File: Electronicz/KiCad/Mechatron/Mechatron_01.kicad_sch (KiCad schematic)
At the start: 47 parts, among them J1 Conn_01x15_Socket, J10 Servo_1, J11 Servo_2, J12 Servo_3, J13 V_ESP32, J14 GND_ESP32, J15 Motor_1, J16 Motor_2, J17 Motor_3, J18 Motor_4, J19 V_LED_2, J2 US_Sensor1, J20 V_LED_1, J21 V_LED_top, J22 GND_LED_top, J23 GND_LED_2, J24 GND_LED_1, J25 SD-Card-Reader, J26 Amplifier, J27 Speaker, J3 US_sensor_2, J4 US_sensor3, J5 US_sensor4, J6 US_sensor5, J7 US_sensor6, J8 GND_Battery, J9 V_Battery_Switch, Q1 LR_LED_Sensors, Q2 LR_3, Q3 LR_2, Q4 LR_1, Q5 LED_top, Q6 LED_2, Q7 LED_1

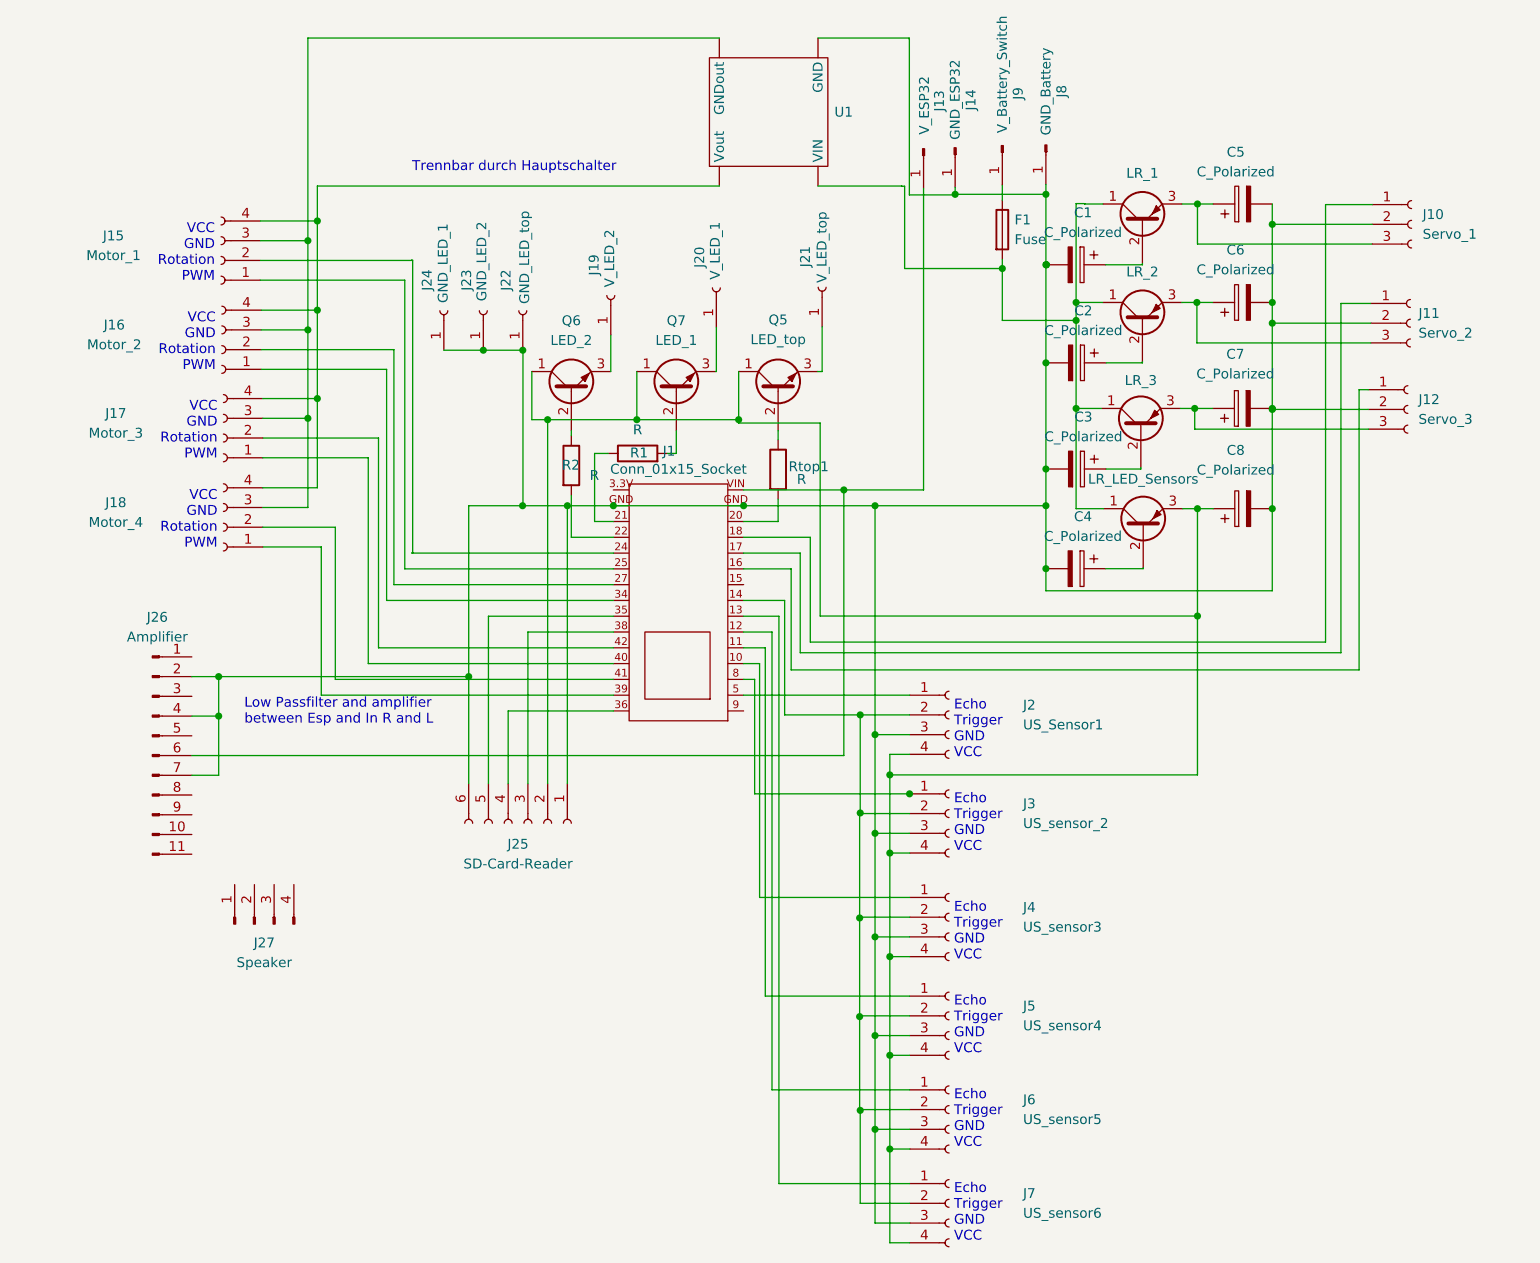
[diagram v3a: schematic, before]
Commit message: add filter and label of the Pin Header
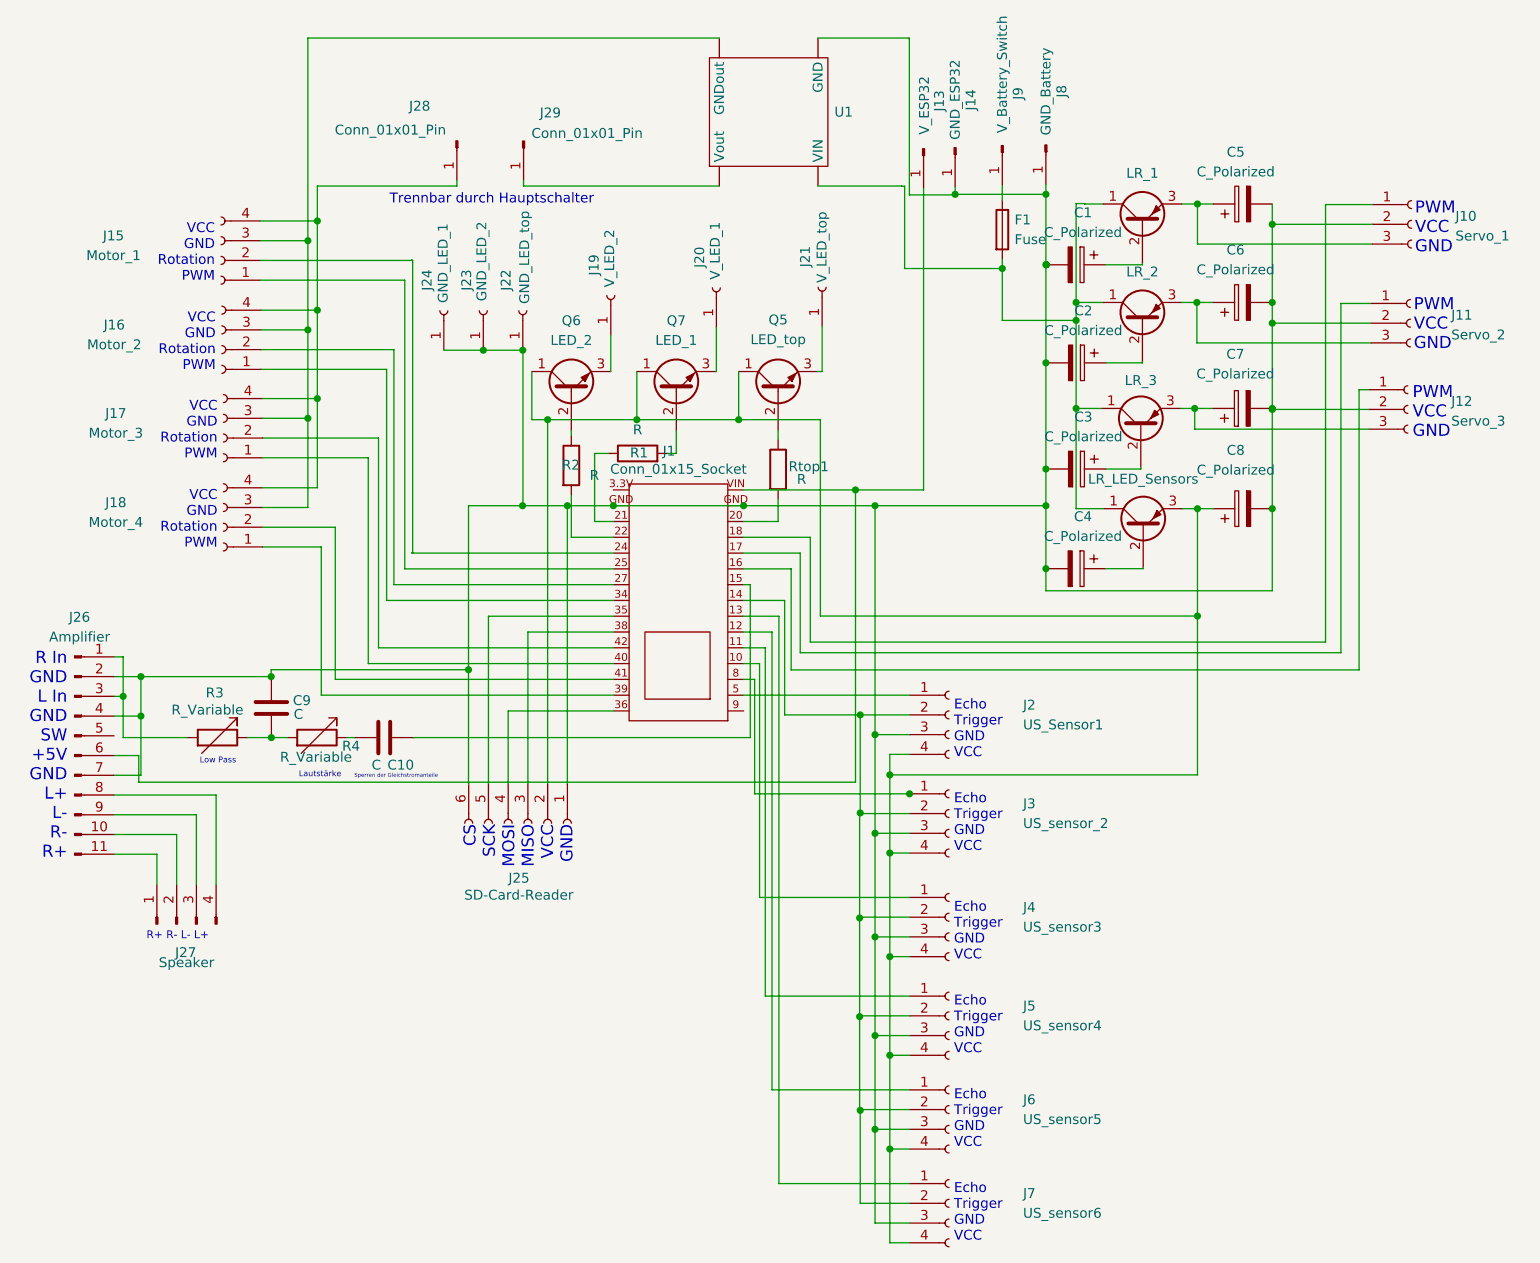
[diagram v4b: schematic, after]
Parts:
- added C10, C9: C, symbol Device:C
- added J28, J29: Conn_01x01_Pin, symbol Connector:Conn_01x01_Pin
- added R3, R4: R_Variable, symbol Device:R_Variable
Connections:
- net at J26.1 (Pin_1): now also J26.3 (Pin_3), R3.2
- net at J26.10 (Pin_10): now also J27.2 (Pin_2)
- net at J26.11 (Pin_11): now also J27.1 (Pin_1)
- net at C1.2, C2.2, C3.2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: now also C9.1
- net at J26.8 (Pin_8): now also J27.4 (Pin_4)
- net at J26.9 (Pin_9): now also J27.3 (Pin_3)
- net at J15.4 (Pin_4), J16.4 (Pin_4), J17.4 (Pin_4)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: now also J28.1 (Pin_1); no longer U1. (Vout)
- net at J1.15: now also C10.1
- new net: C10.2, R4.1
- new net: C9.2, R3.1, R4.2
- new net: J29.1 (Pin_1), U1. (Vout)
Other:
- note added: "CS SCK MOSI MISO VCC GND"
- note added: "Lautstärke"
- note added: "Low Pass"
- note added: "PWM VCC GND"
- note added: "R In GND L In GND SW +5V GND L+ L- R- R+"
- note added: "R+ R- L- L+"
- note added: "Sperren der Gleichstromanteile"
- note removed: "Low Passfilter and amplifier between Esp and In R and L"
- moved on the sheet: J26, J27

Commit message: Platinendesign
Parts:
- removed J26: Amplifier, symbol Connector:Conn_01x11_Pin
- removed J27: Speaker, symbol Connector:Conn_01x04_Pin
- added J26: AUDIOAMP, Connector_PinSocket_2.00mm:PinSocket_1x09_P2.00mm_Vertical, symbol Connector:Conn_01x09_Socket
- added J27: Speaker, Connector_PinHeader_2.54mm:PinHeader_1x02_P2.54mm_Vertical, symbol Connector:Conn_01x02_Pin
- added J30: SW, Connector_PinSocket_2.00mm:PinSocket_1x01_P2.00mm_Vertical, symbol Connector:Conn_01x01_Socket
- C1, C2, C3, C4, C5, C6, C7, C8: footprint (none) -> Capacitor_THT:C_Disc_D4.3mm_W1.9mm_P5.00mm
- C10, C9: footprint (none) -> Capacitor_THT:C_Disc_D3.0mm_W1.6mm_P2.50mm
- F1: footprint (none) -> Fuse:Fuseholder_Clip-5x20mm_Eaton_1A5601-01_Inline_P20.80x6.76mm_D1.70mm_Horizontal
- J28, J29: footprint (none) -> Connector_PinHeader_2.54mm:PinHeader_1x01_P2.54mm_Vertical
- Q1, Q2, Q3, Q4: footprint (none) -> Package_TO_SOT_THT:TO-126-3_Vertical
- R3: footprint (none) -> Potentiometer_THT:Potentiometer_Bourns_3386C_Horizontal
- R4: footprint (none) -> Resistor_THT:R_Axial_DIN0207_L6.3mm_D2.5mm_P10.16mm_Horizontal
- U1: footprint (none) -> Library:Spannungsregler
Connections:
- net at R3.2: now also J26.7 (Pin_7), J26.9 (Pin_9)
- net at C1.2, C2.2, C3.2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: now also U1.2 (GND), J26.3 (Pin_3), J26.6 (Pin_6), J26.8 (Pin_8); no longer U1. (Vout)
- net at J1.VIN, J13.1 (Pin_1): now also J26.4 (Pin_4)
- net at J15.3 (Pin_3), J16.3 (Pin_3), J17.3 (Pin_3)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: now also U1.4 (GNDout); no longer U1. (Vout)
- net at F1.2, Q1.1 (C), Q2.1 (C)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: now also U1.1 (VIN); no longer U1. (Vout)
- net at J29.1 (Pin_1): now also U1.3 (Vout); no longer U1. (Vout)
- new net: J26.1 (Pin_1), J27.1 (Pin_1)
- new net: J26.2 (Pin_2), J27.2 (Pin_2)
- new net: J26.5 (Pin_5), J30.1 (Pin_1)
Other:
- note added: "L- L+"
- note added: "R In GND L In GND SW +5V GND + -"
- note removed: "R In GND L In GND SW +5V GND L+ L- R- R+"
- note removed: "R+ R- L- L+"

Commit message: pcb design
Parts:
- J2: value US_Sensor1 -> Front
- J3: value US_sensor_2 -> Left_Front
- J4: value US_sensor3 -> Left_Back
- J5: value US_sensor4 -> Back
- J6: value US_sensor5 -> Right_Back
- J7: value US_sensor6 -> Right_Front
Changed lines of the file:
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@@
   (junction (at 121.8184 117.983) (diameter 0) (color 0 0 0 0)
   )
-  (junction (at 126.2634 112.903) (diameter 0) (color 0 0 0 0)
-  )
   (junction (at 123.7234 133.858) (diameter 0) (color 0 0 0 0)
   )
@@
     (stroke (width 0) (type default))
   )
-  (wire (pts (xy 106.3244 112.903) (xy 106.3244 98.171))
+  (wire (pts (xy 106.299 112.903) (xy 106.299 98.171))
     (stroke (width 0) (type default))
   )
@@
     (stroke (width 0) (type default))
   )
-  (wire (pts (xy 126.2888 112.903) (xy 126.2634 112.903))
+  (wire (pts (xy 106.299 112.903) (xy 126.2634 112.903))
     (stroke (width 0) (type default))
   )
@@
     (stroke (width 0) (type default))
   )
-  (wire (pts (xy 126.2634 112.903) (xy 106.3244 112.903))
-    (stroke (width 0) (type default))
-  )
   (wire (pts (xy 125.6284 45.2882) (xy 125.6284 34.6964))
     (stroke (width 0) (type default))
@@
     (stroke (width 0) (type default))
   )
-  (wire (pts (xy 106.3244 98.171) (xy 104.902 98.171))
+  (wire (pts (xy 106.299 98.171) (xy 104.902 98.171))
     (stroke (width 0) (type default))
   )
@@
       (effects (font (size 1.27 1.27)) (justify left))
     )
-    (property "Value" "US_sensor4" (at 140.8684 142.748 0)
+    (property "Value" "Back" (at 140.8684 142.748 0)
       (effects (font (size 1.27 1.27)) (justify left))
     )
@@
       (effects (font (size 1.27 1.27)) (justify left))
     )
-    (property "Value" "US_sensor5" (at 140.8684 154.813 0)
+    (property "Value" "Right_Back" (at 140.8684 154.813 0)
       (effects (font (size 1.27 1.27)) (justify left))
     )
@@
       (effects (font (size 1.27 1.27)) (justify left))
     )
-    (property "Value" "US_sensor6" (at 140.8684 166.878 0)
+    (property "Value" "Right_Front" (at 140.8684 166.878 0)
       (effects (font (size 1.27 1.27)) (justify left))
     )
@@
       (effects (font (size 1.27 1.27)) (justify left))
     )
-    (property "Value" "US_sensor_2" (at 140.8684 116.713 0)
+    (property "Value" "Left_Front" (at 140.8684 116.713 0)
       (effects (font (size 1.27 1.27)) (justify left))
     )
@@
       (effects (font (size 1.27 1.27)) (justify left))
     )
-    (property "Value" "US_Sensor1" (at 140.8684 104.013 0)
+    (property "Value" "Front" (at 140.8684 104.013 0)
       (effects (font (size 1.27 1.27)) (justify left))
     )
@@
       (effects (font (size 1.27 1.27)) (justify left))
     )
-    (property "Value" "US_sensor3" (at 140.8684 130.048 0)
-      (effects (font (size 1.27 1.27)) (justify left))
-    )
+    (property "Value" "Left_Back" (at 140.8684 130.048 0)
+      (effects (font (size 1.27 1.27)) (justify left))
+    )

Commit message: Create PCB
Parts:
- J25: footprint Connector_PinSocket_2.54mm:PinSocket_1x06_P2.54mm_Vertical -> Library:SDcard_reader
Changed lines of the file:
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@@
+    (stroke (width 0) (type default))
+  )
+  (wire (pts (xy 114.4778 15.621) (xy 126.2126 15.621))
     (stroke (width 0) (type default))
   )
@@
   )
   (wire (pts (xy 121.8184 131.318) (xy 121.8184 117.983))
-    (stroke (width 0) (type default))
-  )
-  (wire (pts (xy 126.2126 15.621) (xy 114.4778 15.621))
     (stroke (width 0) (type default))
   )
@@
       (effects (font (size 1.27 1.27)))
     )
-    (property "Footprint" "Connector_PinSocket_2.54mm:PinSocket_1x06_P2.54mm_Vertical" (at 77.1398 116.6876 0)
-      (effects (font (size 1.27 1.27)) hide)
+    (property "Footprint" "Library:SDcard_reader" (at 85.979 116.3828 0)
+      (effects (font (size 1.27 1.27)))
     )
     (property "Datasheet" "~" (at 77.1398 116.6876 0)

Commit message: Finishing PCB
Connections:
- net at C1.2, C2.2, C3.2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: now also J10.3 (Pin_3), J11.3 (Pin_3), J12.3 (Pin_3), Q1.2 (B), Q2.2 (B), Q3.2 (B), Q4.2 (B), Q5.3 (E), Q6.3 (E), Q7.3 (E); no longer J10.2 (Pin_2), J11.2 (Pin_2), J12.2 (Pin_2), J22.1 (Pin_1), J23.1 (Pin_1), J24.1 (Pin_1)
- net at C8.1, J2.4 (Pin_4), J25.2 (Pin_2)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: now also J19.1 (Pin_1), J20.1 (Pin_1), J21.1 (Pin_1); no longer Q5.1 (C), Q6.1 (C), Q7.1 (C)
- net at C6.1, Q3.3 (E): now also J11.2 (Pin_2); no longer J11.3 (Pin_3)
- net at C1.1: now also C2.1, C3.1, C4.1, F1.2, Q1.1 (C), Q2.1 (C), Q3.1 (C), Q4.1 (C), U1.1 (VIN); no longer Q4.2 (B)
- net at C5.1, Q4.3 (E): now also J10.2 (Pin_2); no longer J10.3 (Pin_3)
- net at C7.1, Q2.3 (E): now also J12.2 (Pin_2); no longer J12.3 (Pin_3)
- new net: J24.1 (Pin_1), Q7.1 (C)
- new net: J22.1 (Pin_1), Q5.1 (C)
- new net: J23.1 (Pin_1), Q6.1 (C)
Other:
- moved on the sheet: C7, J19, J20, J21, J22, J23, J24
